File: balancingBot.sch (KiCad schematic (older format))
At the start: 31 parts, among them P1 CONN_01X02, P2 CONN_01X02, P3 CONN_01X02, P4 CONN_01X02, P5 CONN_01X02, P6 CONN_01X02, SW1 SW_DIP_x01, U1 DRV8825, U2 DRV8825, U3 WRL-00691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

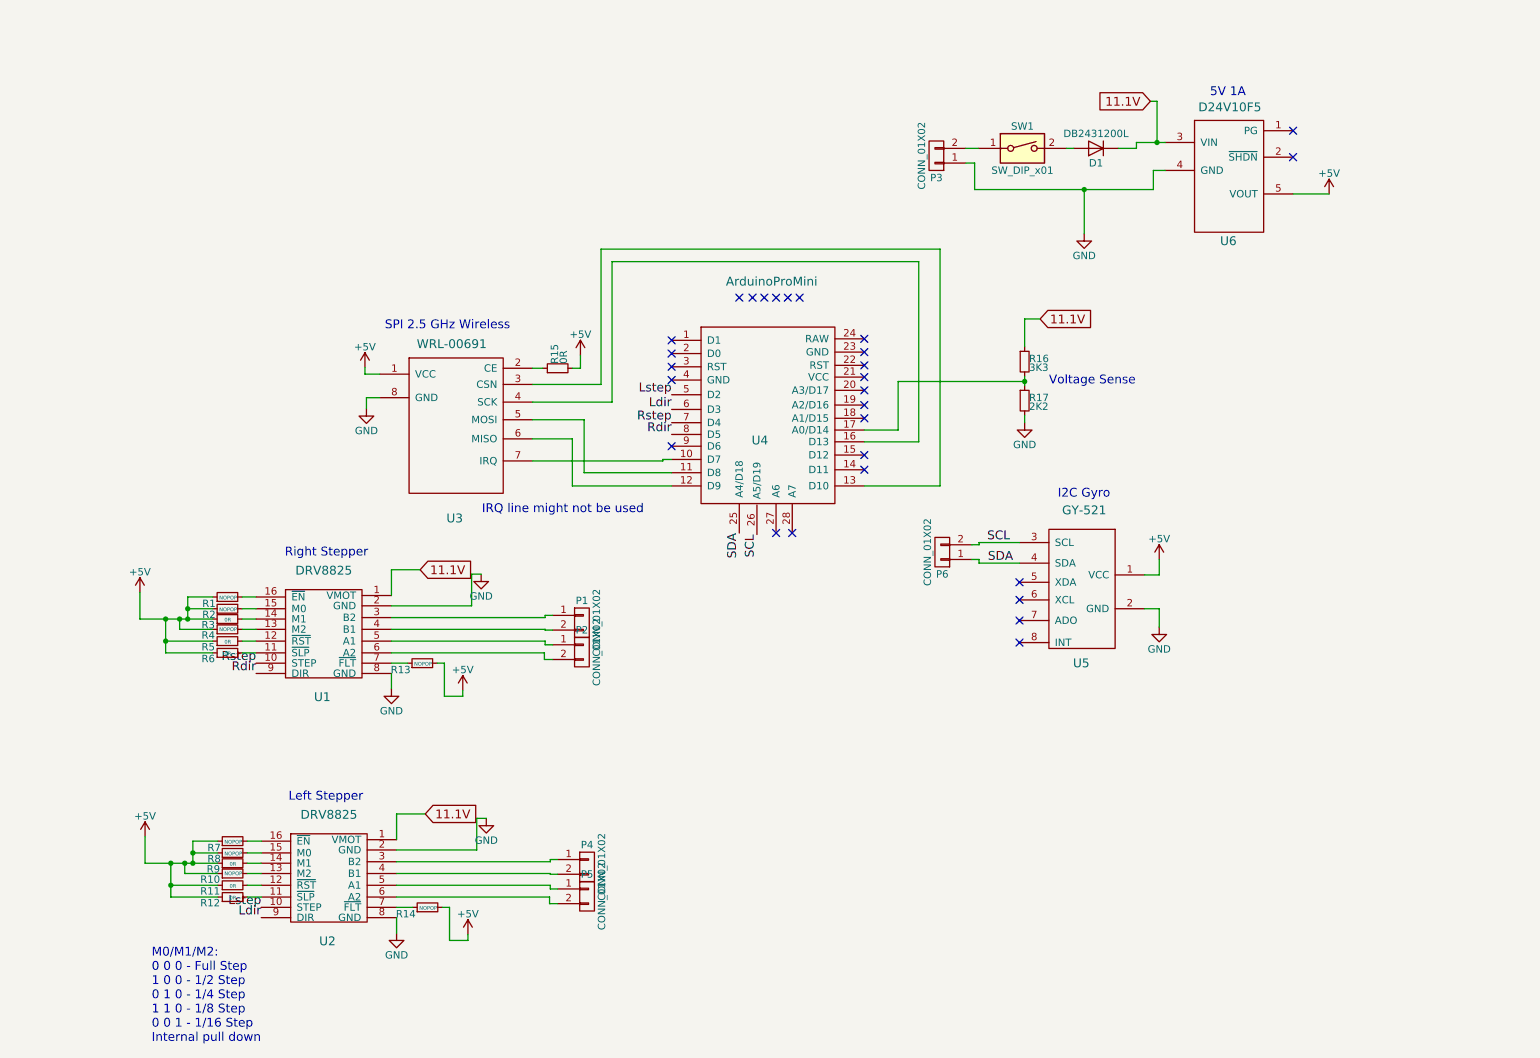
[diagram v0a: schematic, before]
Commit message: added caps to motor driver and changed diode to 1N4001
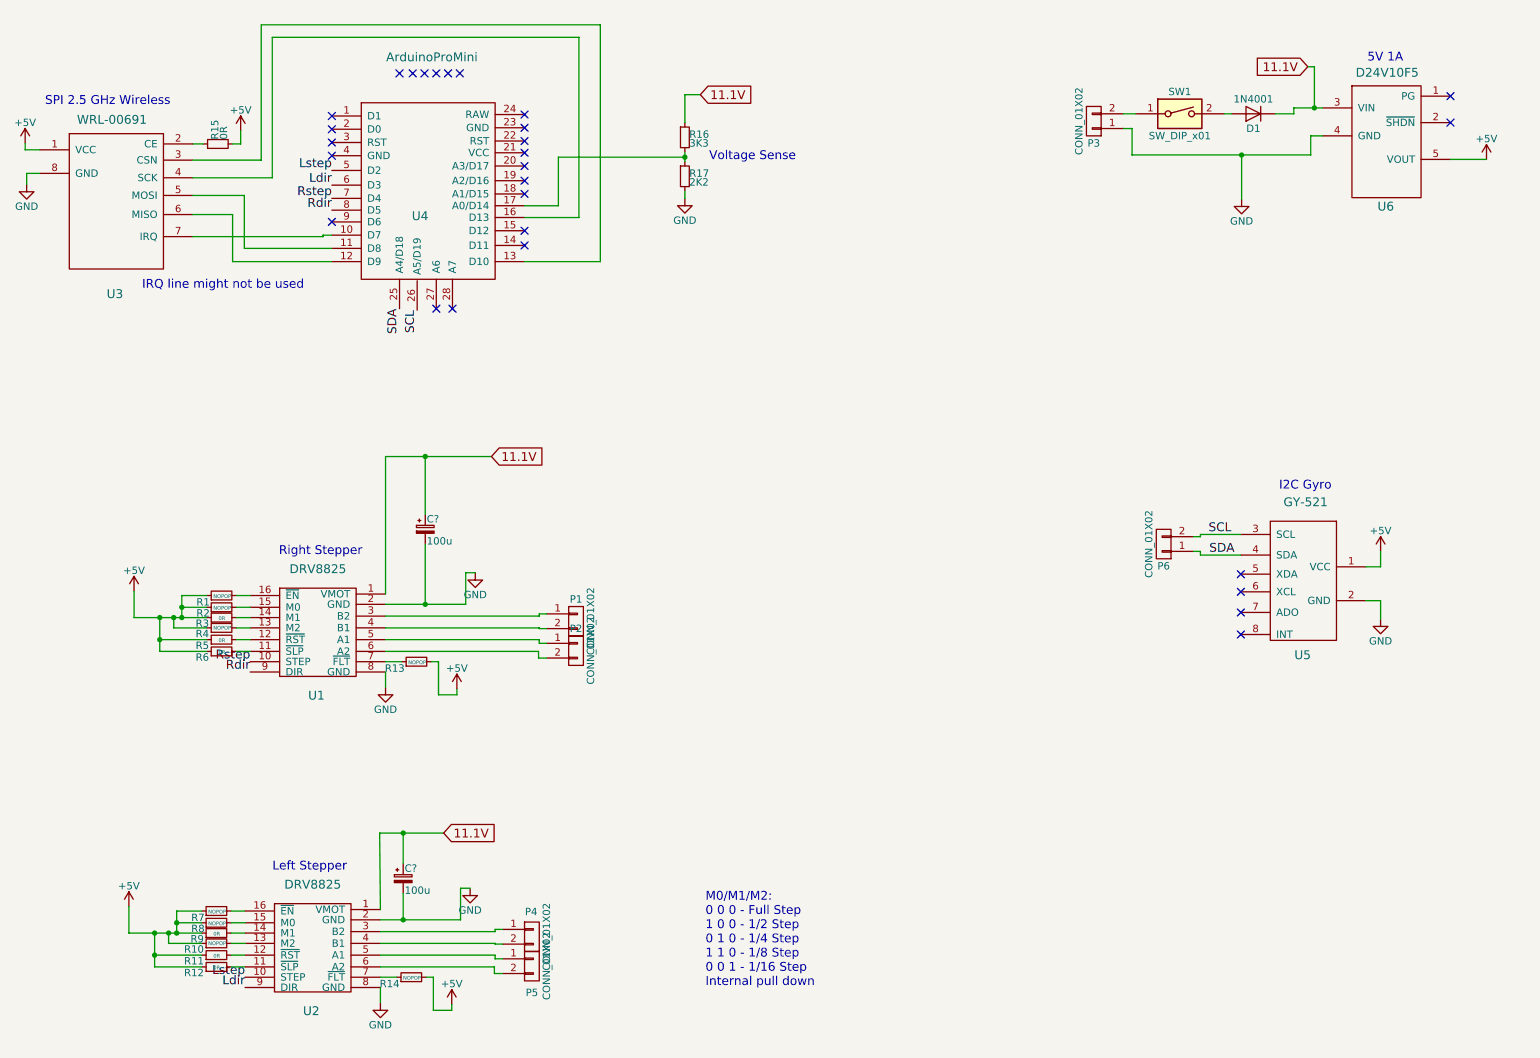
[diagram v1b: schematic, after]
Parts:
- added C? (x2): 100u, symbol CP_Small
- D1: value DB2431200L -> 1N4001
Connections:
- net 11.1V: now also C?.1, C?.1
- net GND: now also C?.2, C?.2
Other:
- moved on the sheet: D1, P1, P2, P3, P4, P5, P6, R1, R10, R11, R12, R13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

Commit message: organized schematic
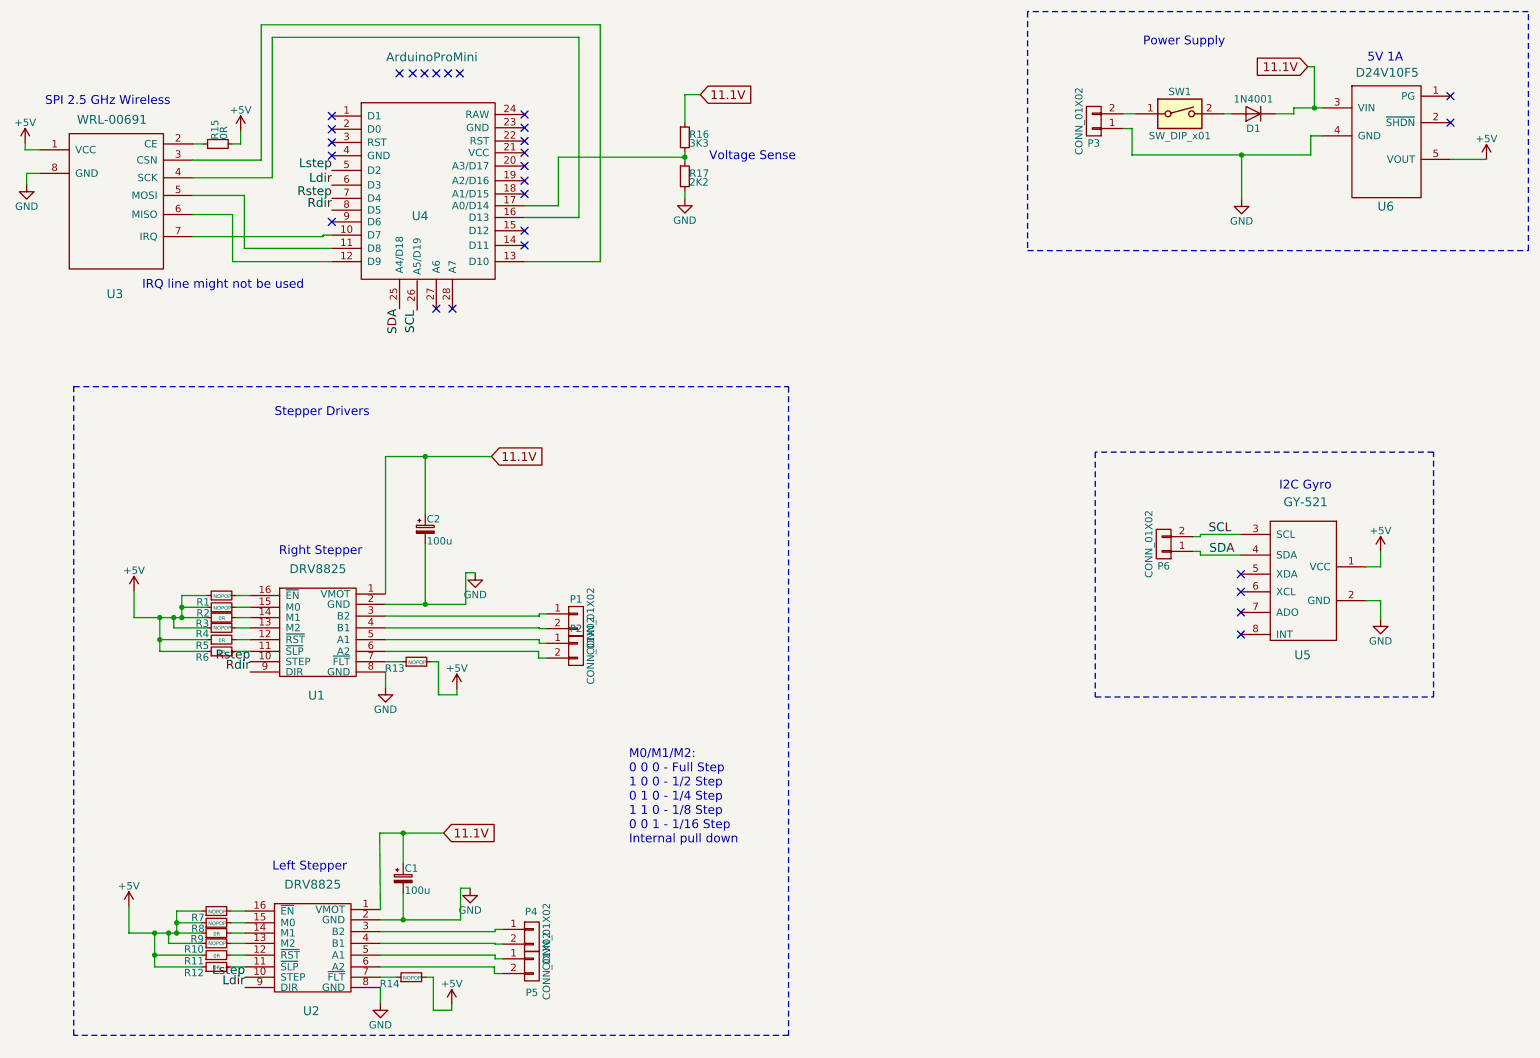
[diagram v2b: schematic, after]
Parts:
- gave numbers to parts that had none: 2
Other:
- note added: "Power Supply"
- note added: "Stepper Drivers"
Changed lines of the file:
@@
 	1    0    0    -1
 $EndComp
-Text Notes 5335 7250 0    60   ~ 0
+Text Notes 4815 6280 0    60   ~ 0
 M0/M1/M2:\n0 0 0 - Full Step\n1 0 0 - 1/2 Step\n0 1 0 - 1/4 Step\n1 1 0 - 1/8 Step\n0 0 1 - 1/16 Step\nInternal pull down\n
 $Comp
@@
 	3120 6200 3120 6210
 $Comp
-L CP_Small C?
+L CP_Small C1
 U 1 1 597F365E
 P 3280 6510
-F 0 "C?" H 3290 6580 50  0000 L CNN
+F 0 "C1" H 3290 6580 50  0000 L CNN
 F 1 "100u" H 3290 6430 50  0000 L CNN
 F 2 "" H 3280 6510 50  0000 C CNN
@@
 	3160 3640 3880 3640
 $Comp
-L CP_Small C?
+L CP_Small C2
 U 1 1 597F6244
 P 3430 4135
-F 0 "C?" H 3440 4205 50  0000 L CNN
+F 0 "C2" H 3440 4205 50  0000 L CNN
 F 1 "100u" H 3440 4055 50  0000 L CNN
 F 2 "" H 3430 4135 50  0000 C CNN
@@
 Connection ~ 3430 4645
 Connection ~ 3430 3640
+Wire Notes Line
+	7525 615  7525 2240
+Wire Notes Line
+	7525 2240 10930 2240
+Wire Notes Line
+	10930 2240 10930 615
+Wire Notes Line
+	10930 615  7525 615
+Text Notes 8310 855  0    60   ~ 0
+Power Supply
+Wire Notes Line
+	7985 3610 7985 5275
+Wire Notes Line
+	7985 5275 10285 5275
+Wire Notes Line
+	10285 5275 10285 3610
+Wire Notes Line
+	10285 3610 7985 3610
+Wire Notes Line
+	1040 3165 5900 3165
+Wire Notes Line
+	5900 3165 5900 7575
+Wire Notes Line
+	5900 7575 1040 7575
+Wire Notes Line
+	1040 7575 1040 3160
+Text Notes 2405 3375 0    60   ~ 0
+Stepper Drivers
 $EndSCHEMATC

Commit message: corrected SPI connections
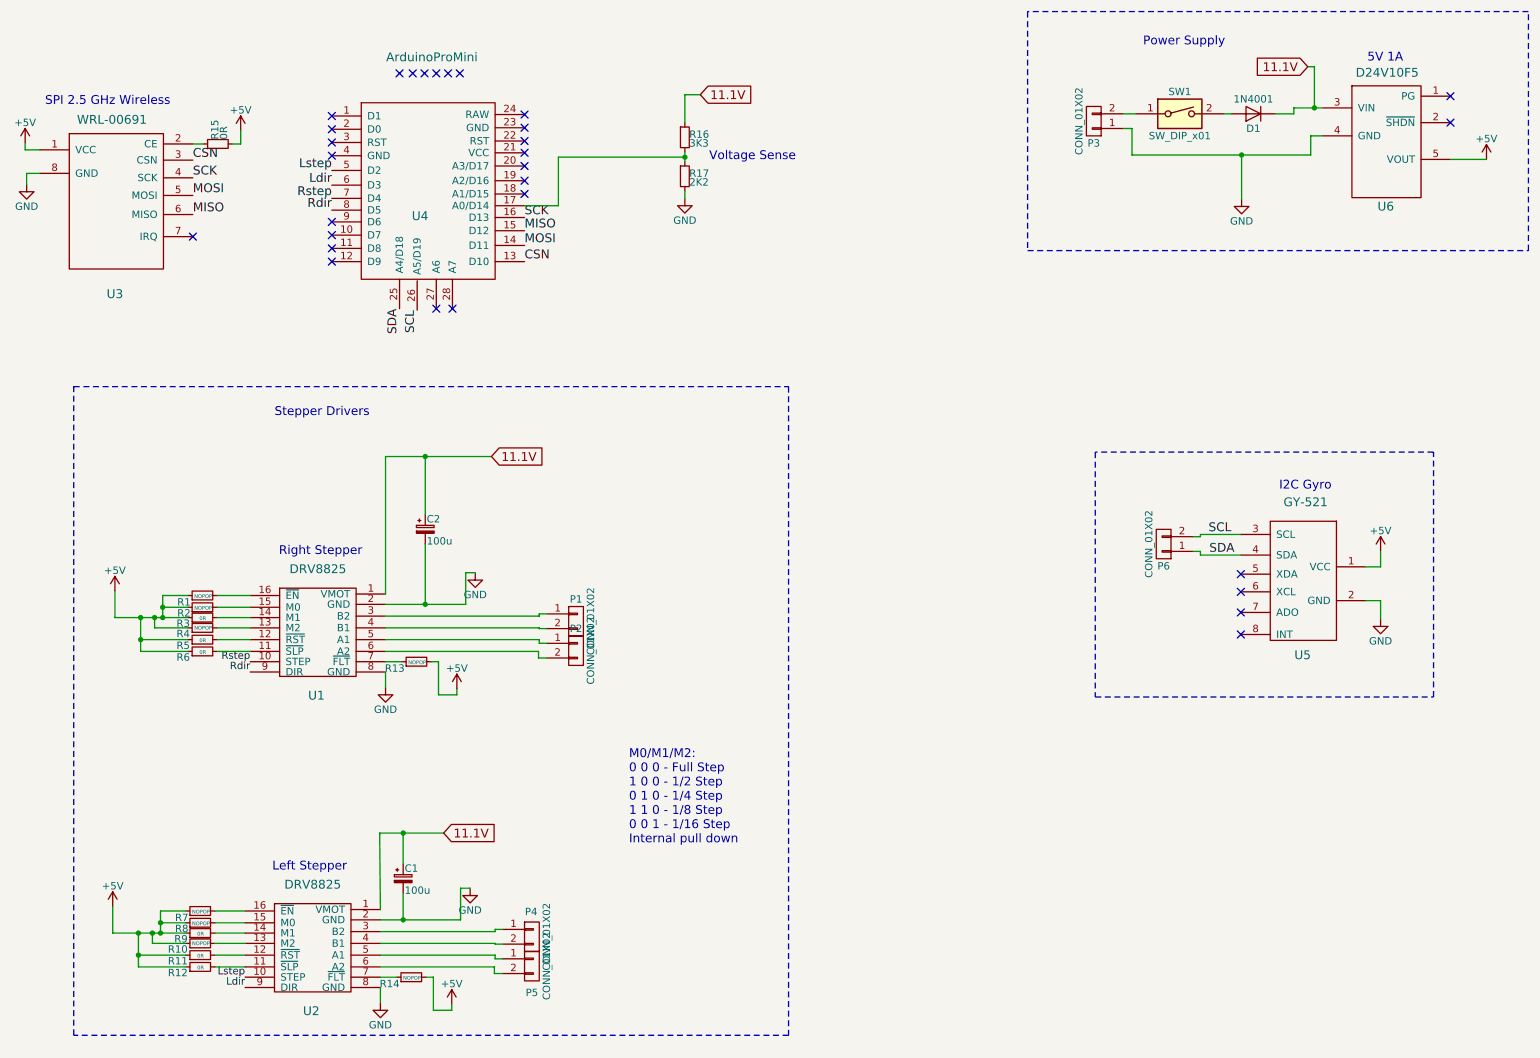
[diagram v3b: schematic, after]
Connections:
- net at U4.10 (D7): no longer U3.7 (IRQ)
- net at U4.11 (D8): no longer U3.5 (MOSI)
- net at U4.12 (D9): no longer U3.6 (MISO)
- net CSN: now reaches U3.3 (CSN), U4.13 (D10)
- net MOSI: now reaches U4.14 (D11)
- net MOSI: now also U3.5 (MOSI)
- net MISO: now reaches U4.15 (D12)
- net MISO: now also U3.6 (MISO)
- net SCK: now reaches U3.4 (SCK), U4.16 (D13)
- no-connect marks 28 -> 30
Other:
- note removed: "IRQ line might not be used"
- moved on the sheet: R1, R10, R11, R12, R2, R3, R4, R5, R6, R7, R8, R9
